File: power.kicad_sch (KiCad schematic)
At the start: 45 parts, among them J10 Conn_01x02, J11 Solar_Cell, J2 USB_C_Receptacle_USB2.0_14P, J9 Battery_Cell, Q1 AO4882, Q3 AO4882, U2 BQ25798, U5 TPS6282x

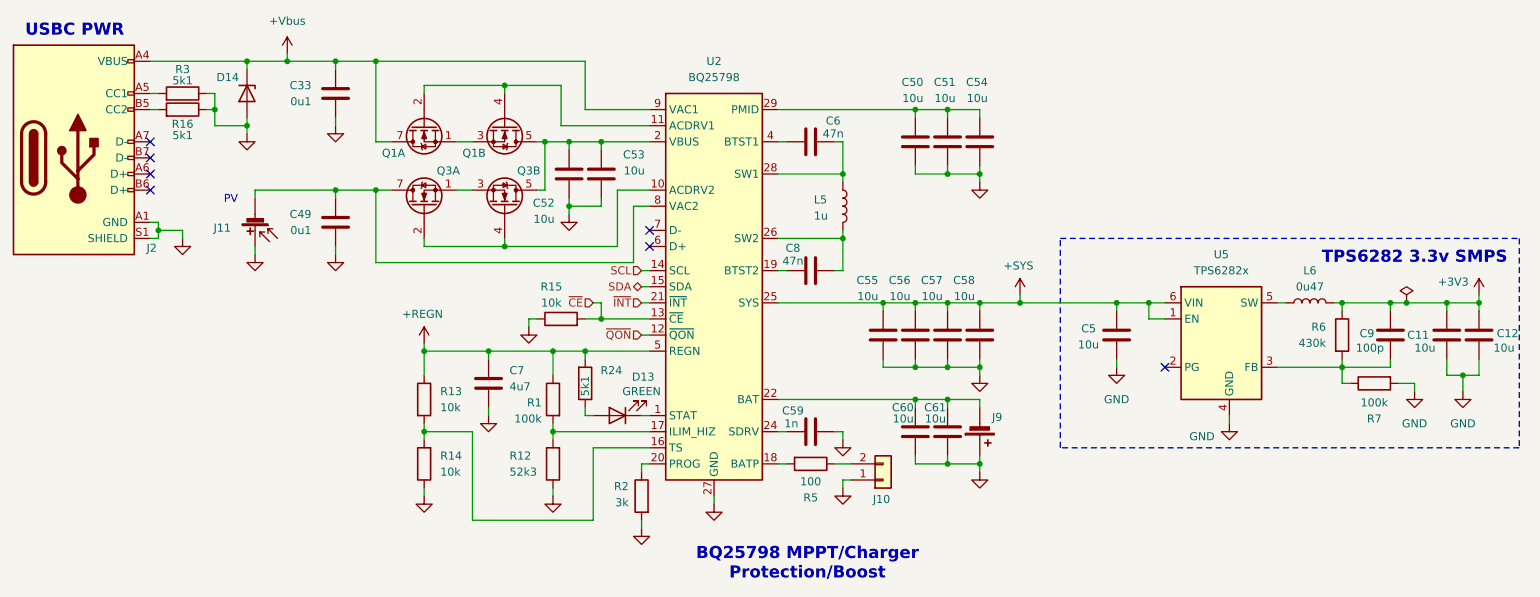
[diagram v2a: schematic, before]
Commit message: schem: add current measure jumpers
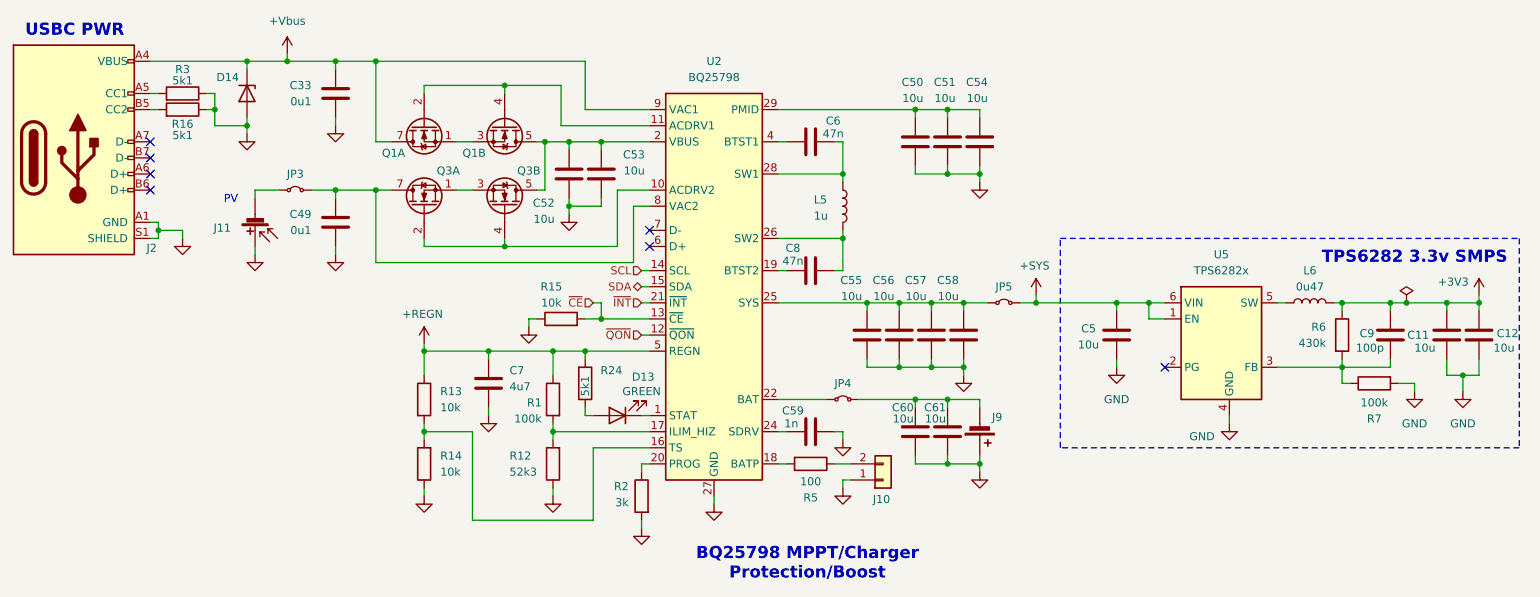
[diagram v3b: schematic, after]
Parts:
- added JP3, JP4, JP5: Jumper_2_Small_Bridged, symbol Jumper:Jumper_2_Small_Bridged
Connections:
- net +SYS: now also JP5.2 (B); no longer C55.1, C56.1, C57.1, C58.1, U2.25 (SYS)
- net at C60.1, C61.1, J9.2 (-): now also JP4.2 (B); no longer U2.22 (BAT), U2.23 (BAT)
- net at C49.1, Q3.7 (D1), Q3.8 (D1)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: now also JP3.2 (B); no longer J11.2 (-)
- new net: C55.1, C56.1, C57.1, C58.1, JP5.1 (A), U2.25 (SYS)
- new net: JP4.1 (A), U2.22 (BAT), U2.23 (BAT)
- new net: J11.2 (-), JP3.1 (A)
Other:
- moved on the sheet: C55, C56, C57, C58

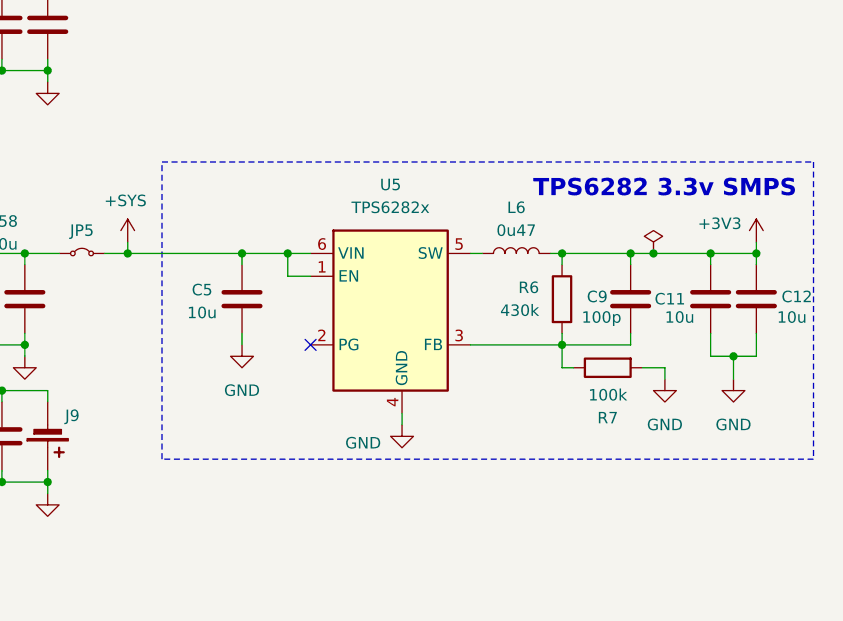
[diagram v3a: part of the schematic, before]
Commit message: schem: add no connects
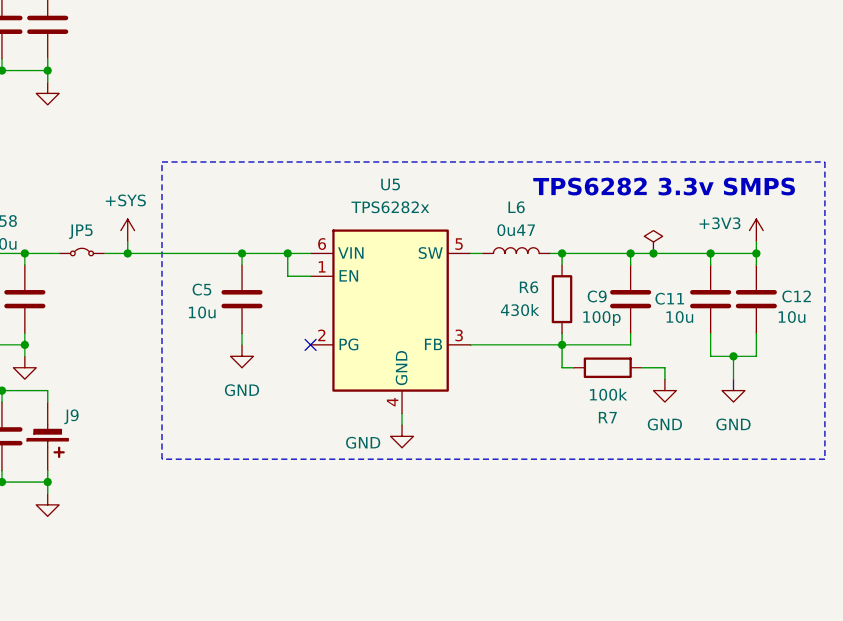
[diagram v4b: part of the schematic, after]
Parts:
- C6, C8: footprint (none) -> Capacitor_SMD:C_0402_1005Metric
- C7: footprint (none) -> Capacitor_SMD:C_0603_1608Metric
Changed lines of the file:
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@@
 	(rectangle
 		(start 203.2 92.71)
-		(end 275.59 125.73)
+		(end 276.86 125.73)
 		(stroke
 			(width 0)
@@
 			)
 		)
-		(property "Footprint" ""
+		(property "Footprint" "Capacitor_SMD:C_0402_1005Metric"
 			(at 167.64 98.7552 0)
 			(hide yes)
@@
 			)
 		)
-		(property "Footprint" ""
+		(property "Footprint" "Capacitor_SMD:C_0402_1005Metric"
 			(at 167.64 76.5048 0)
 			(hide yes)
@@
 			)
 		)
-		(property "Footprint" ""
+		(property "Footprint" "Capacitor_SMD:C_0603_1608Metric"
 			(at 113.9952 119.38 0)
 			(hide yes)

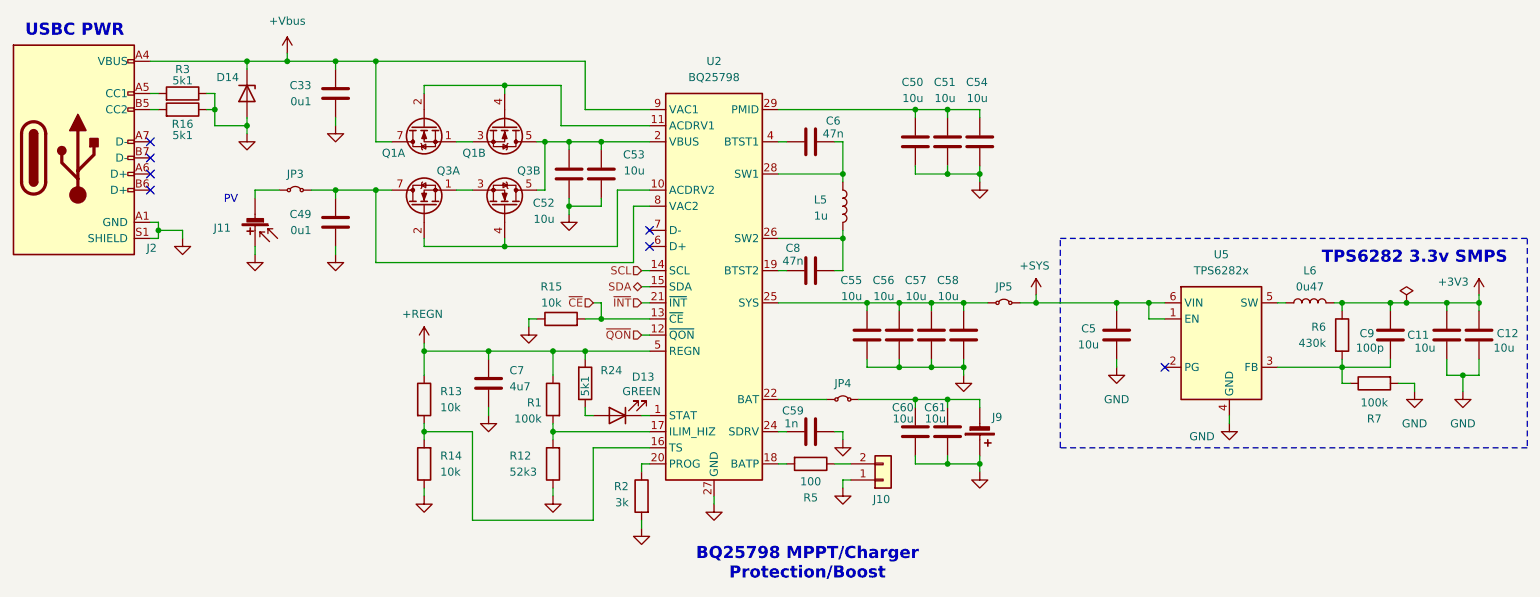
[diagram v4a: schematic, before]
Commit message: schem: add test points
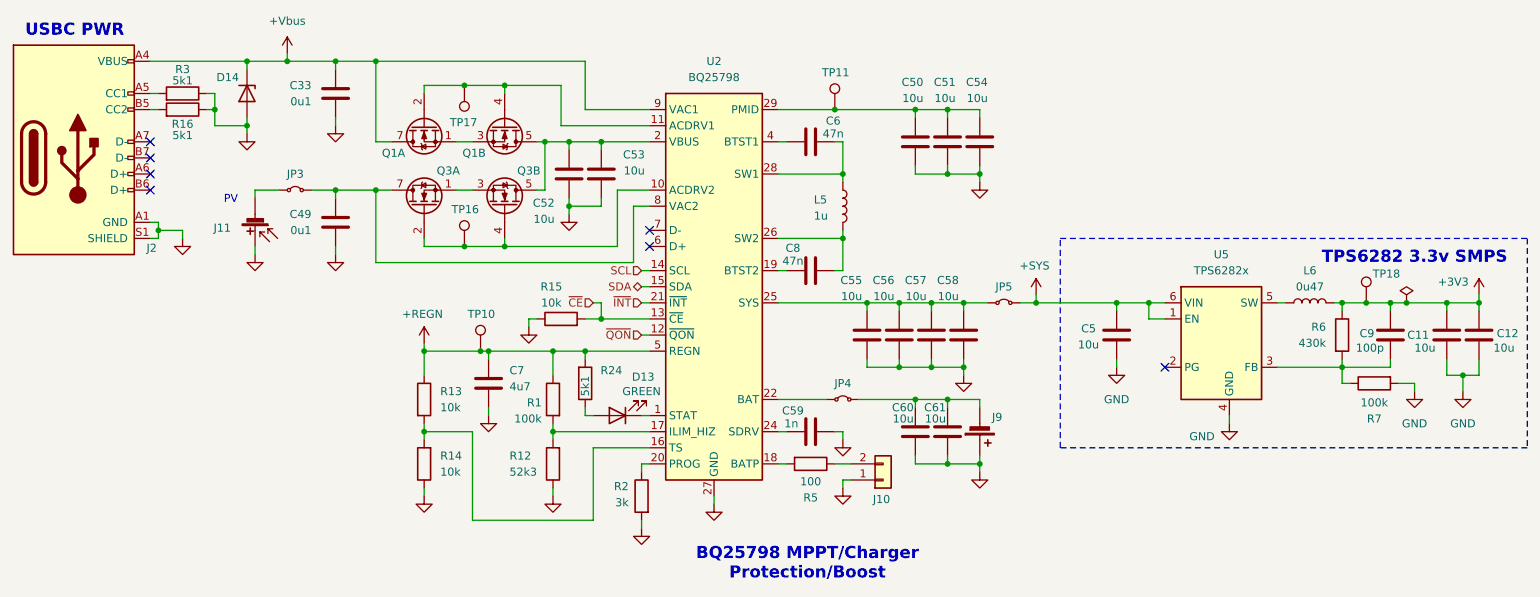
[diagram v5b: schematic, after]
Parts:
- added TP10, TP11, TP16, TP17, TP18: TestPoint, TestPoint:TestPoint_Pad_D2.0mm, symbol Connector:TestPoint
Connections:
- net +3V3: now also TP18.1
- net +REGN: now also TP10.1
- net at C50.1, C51.1, C54.1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: now also TP11.1
- net at Q3.2 (G1), Q3.4 (G2), U2.10 (ACDRV2): now also TP16.1
- net at Q1.2 (G1), Q1.4 (G2), U2.11 (ACDRV1): now also TP17.1

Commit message: schem: run and fix ERC
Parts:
- L6: footprint Pers:TDK_TFM201610ALC -> GLCS:TDK_TFM201610ALC
- U5: footprint Pers:Texas_VSON-6_1.5x1.5mm_P0.5mm_DMQ0006A -> GLCS:Texas_VSON-6_1.5x1.5mm_P0.5mm_DMQ0006A; symbol Pers:TPS6282x -> GLCS:TPS6282x
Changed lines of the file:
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@@
 	)
 	(junction
+		(at 63.5 91.44)
+		(diameter 0)
+		(color 0 0 0 0)
+	)
+	(junction
 		(at 190.5 82.55)
 		(diameter 0)
@@
 		(color 0 0 0 0)
 	)
+	(junction
+		(at 123.19 77.47)
+		(diameter 0)
+		(color 0 0 0 0)
+	)
 	(no_connect
 		(at 138.43 93.98)
@@
 	(wire
 		(pts
+			(xy 123.19 77.47) (xy 125.73 77.47)
+		)
+		(stroke
+			(width 0)
+			(type default)
+		)
+	)
+	(wire
+		(pts
 			(xy 182.88 113.03) (xy 177.8 113.03)
 		)
@@
 	(wire
 		(pts
+			(xy 63.5 91.44) (xy 64.77 91.44)
+		)
+		(stroke
+			(width 0)
+			(type default)
+		)
+	)
+	(wire
+		(pts
 			(xy 102.87 93.98) (xy 102.87 92.71)
 		)
@@
 	(wire
 		(pts
-			(xy 121.92 77.47) (xy 125.73 77.47)
+			(xy 121.92 77.47) (xy 123.19 77.47)
 		)
 		(stroke
@@
 	(wire
 		(pts
-			(xy 60.96 91.44) (xy 64.77 91.44)
+			(xy 60.96 91.44) (xy 63.5 91.44)
 		)
 		(stroke
@@
 	)
 	(symbol
+		(lib_id "power:PWR_FLAG")
+		(at 123.19 77.47 0)
+		(unit 1)
+		(body_style 1)
+		(exclude_from_sim no)
+		(in_bom yes)
+		(on_board yes)
+		(in_pos_files yes)
+		(dnp no)
+		(fields_autoplaced yes)
+		(property "Reference" "#FLG03"
+			(at 123.19 75.565 0)
+			(hide yes)
+			(show_name no)
+			(do_not_autoplace no)
+			(effects
+				(font
+					(size 1.27 1.27)
+				)
+			)
+		)
+		(property "Value" "PWR_FLAG"
+			(at 123.19 72.39 0)
+			(hide yes)
+			(show_name no)
+			(do_not_autoplace no)
+			(effects
+				(font
+					(size 1.27 1.27)
+				)
+			)
+		)
+		(property "Footprint" ""
+			(at 123.19 77.47 0)
+			(hide yes)
+			(show_name no)
+			(do_not_autoplace no)
+			(effects
+				(font
+					(size 1.27 1.27)
+				)
+			)
+		)
+		(property "Datasheet" ""
+			(at 123.19 77.47 0)
+			(hide yes)
+			(show_name no)
+			(do_not_autoplace no)
+			(effects
+				(font
+					(size 1.27 1.27)
+				)
+			)
+		)
+		(property "Description" "Special symbol for telling ERC where power comes from"
+			(at 123.19 77.47 0)
+			(hide yes)
+			(show_name no)
+			(do_not_autoplace no)
+			(effects
+				(font
+					(size 1.27 1.27)
+				)
+			)
+		)
+		(pin "1"
+		)
+		(instances
+			(project "carte-meteo-lora-1"
+				(path "/13f499c2-4dc3-4e2c-8cf4-c7d5e00eb573/9999b4d2-cbfb-4c4d-87a4-97a3463f3d3b"
+					(reference "#FLG03")
+					(unit 1)
+				)
+			)
+		)
+	)
+	(symbol
 		(lib_id "power:VBUS")
 		(at 81.28 63.5 0)
@@
 			)
 		)
-		(property "Footprint" "Pers:TDK_TFM201610ALC"
+		(property "Footprint" "GLCS:TDK_TFM201610ALC"
 			(at 242.57 102.87 0)
 			(hide yes)
@@
 	)
 	(symbol
+		(lib_id "power:PWR_FLAG")
+		(at 63.5 91.44 0)
+		(unit 1)
+		(body_style 1)
+		(exclude_from_sim no)
+		(in_bom yes)
+		(on_board yes)
+		(in_pos_files yes)
+		(dnp no)
+		(fields_autoplaced yes)
+		(property "Reference" "#FLG05"
+			(at 63.5 89.535 0)
+			(hide yes)
+			(show_name no)
+			(do_not_autoplace no)
+			(effects
+				(font
+					(size 1.27 1.27)
+				)
+			)
+		)
+		(property "Value" "PWR_FLAG"
+			(at 63.5 86.36 0)
+			(hide yes)
+			(show_name no)
+			(do_not_autoplace no)
+			(effects
+				(font
+					(size 1.27 1.27)
+				)
+			)
+		)
+		(property "Footprint" ""
+			(at 63.5 91.44 0)
+			(hide yes)
+			(show_name no)
+			(do_not_autoplace no)
+			(effects
+				(font
+					(size 1.27 1.27)
+				)
+			)
+		)
+		(property "Datasheet" ""
+			(at 63.5 91.44 0)
+			(hide yes)
+			(show_name no)
+			(do_not_autoplace no)
+			(effects
+				(font
+					(size 1.27 1.27)
+				)
+			)
+		)
+		(property "Description" "Special symbol for telling ERC where power comes from"
+			(at 63.5 91.44 0)
+			(hide yes)
+			(show_name no)
+			(do_not_autoplace no)
+			(effects
+				(font
+					(size 1.27 1.27)
+				)
+			)
+		)
+		(pin "1"
+		)
+		(instances
+			(project "carte-meteo-lora-1"
+				(path "/13f499c2-4dc3-4e2c-8cf4-c7d5e00eb573/9999b4d2-cbfb-4c4d-87a4-97a3463f3d3b"
+					(reference "#FLG05")
+					(unit 1)
+				)
+			)
+		)
+	)
+	(symbol
 		(lib_id "Device:C")
 		(at 125.73 82.55 0)
@@
 	)
 	(symbol
-		(lib_id "Pers:TPS6282x")
+		(lib_id "GLCS:TPS6282x")
 		(at 229.87 110.49 0)
 		(unit 1)
@@
 			)
 		)
-		(property "Footprint" "Pers:Texas_VSON-6_1.5x1.5mm_P0.5mm_DMQ0006A"
+		(property "Footprint" "GLCS:Texas_VSON-6_1.5x1.5mm_P0.5mm_DMQ0006A"
 			(at 233.68 119.38 0)
 			(hide yes)
